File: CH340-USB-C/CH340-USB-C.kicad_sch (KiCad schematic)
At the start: 18 parts, among them J1 USB_C_Receptacle_USB2.0, J2 Conn_01x04_MountingPin, SW1 SW_Push_SPDT, U1 XC6206PxxxMR, U2 CH340N

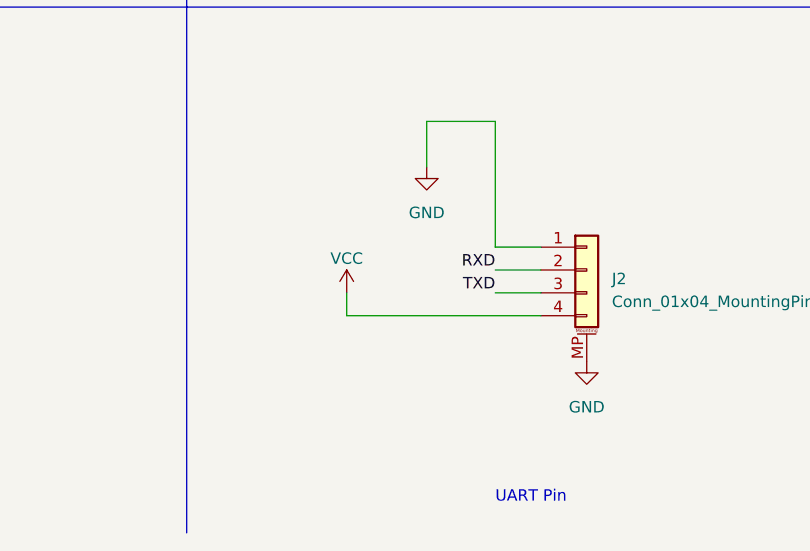
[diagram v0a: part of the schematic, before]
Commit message: 新增
1.可以選擇是否輸出電源(預設"不輸出")
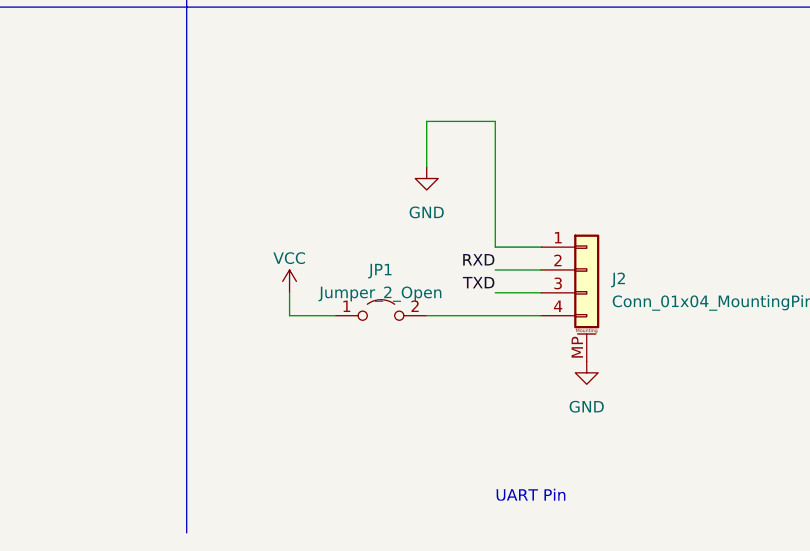
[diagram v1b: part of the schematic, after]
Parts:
- added JP1: Jumper_2_Open, Jumper:SolderJumper-2_P1.3mm_Open_RoundedPad1.0x1.5mm, symbol Jumper:Jumper_2_Open
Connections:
- net VCC: now also JP1.1 (A); no longer J2.4 (Pin_4)
- new net: J2.4 (Pin_4), JP1.2 (B)
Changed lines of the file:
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@@
     (stroke (width 0) (type solid))
   )
-  (wire (pts (xy 115.57 171.45) (xy 115.57 173.99))
+  (wire (pts (xy 109.22 171.45) (xy 109.22 173.99))
     (stroke (width 0) (type default))
   )
@@
     (stroke (width 0) (type default))
   )
+  (wire (pts (xy 114.3 173.99) (xy 109.22 173.99))
+    (stroke (width 0) (type default))
+  )
   (wire (pts (xy 48.26 35.56) (xy 60.96 35.56))
     (stroke (width 0) (type solid))
@@
     (stroke (width 0) (type solid))
   )
-  (wire (pts (xy 137.16 173.99) (xy 115.57 173.99))
+  (wire (pts (xy 137.16 173.99) (xy 124.46 173.99))
     (stroke (width 0) (type default))
   )
@@
     )
   )
+  (symbol (lib_id "Jumper:Jumper_2_Open") (at 119.38 173.99 0) (unit 1)
+    (in_bom yes) (on_board yes) (dnp no) (fields_autoplaced)
+    (property "Reference" "JP1" (at 119.38 168.91 0)
+      (effects (font (size 1.27 1.27)))
+    )
+    (property "Value" "Jumper_2_Open" (at 119.38 171.45 0)
+      (effects (font (size 1.27 1.27)))
+    )
+    (property "Footprint" "Jumper:SolderJumper-2_P1.3mm_Open_RoundedPad1.0x1.5mm" (at 119.38 173.99 0)
+      (effects (font (size 1.27 1.27)) hide)
+    )
+    (property "Datasheet" "~" (at 119.38 173.99 0)
+      (effects (font (size 1.27 1.27)) hide)
+    )
+    (pin "1")
+    (pin "2")
+    (instances
+      (project "CH340-USB-C"
+        (path "/e63e39d7-6ac0-4ffd-8aa3-1841a4541b55"
+          (reference "JP1") (unit 1)
+        )
+      )
+    )
+  )
   (symbol (lib_id "power:GND") (at 142.24 179.07 0) (unit 1)
     (in_bom yes) (on_board yes) (dnp no) (fields_autoplaced)
@@
     )
   )
-  (symbol (lib_id "power:VCC") (at 115.57 171.45 0) (unit 1)
+  (symbol (lib_id "power:VCC") (at 109.22 171.45 0) (unit 1)
     (in_bom yes) (on_board yes) (dnp no) (fields_autoplaced)
-    (property "Reference" "#PWR017" (at 115.57 175.26 0)
-      (effects (font (size 1.27 1.27)) hide)
-    )
-    (property "Value" "VCC" (at 115.57 167.64 0)
-      (effects (font (size 1.27 1.27)))
-    )
-    (property "Footprint" "" (at 115.57 171.45 0)
-      (effects (font (size 1.27 1.27)) hide)
-    )
-    (property "Datasheet" "" (at 115.57 171.45 0)
-      (effects (font (size 1.27 1.27)) hide)
-    )
+    (property "Reference" "#PWR017" (at 109.22 175.26 0)
+      (effects (font (size 1.27 1.27)) hide)
+    )
+    (property "Value" "VCC" (at 109.22 167.64 0)
+      (effects (font (size 1.27 1.27)))
+    )
+    (property "Footprint" "" (at 109.22 171.45 0)
+      (effects (font (size 1.27 1.27)) hide)
+    )
+    (property "Datasheet" "" (at 109.22 171.45 0)
+      (effects (font (size 1.27 1.27)) hide)
+    )

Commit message: 增加絲印
增加公司名稱及腳位名稱
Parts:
- C3, C4: LCSC (none) -> C49678
- JP1, SW1: now left out of the parts list
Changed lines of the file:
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@@
   )
   (symbol (lib_id "Jumper:Jumper_2_Open") (at 119.38 173.99 0) (unit 1)
-    (in_bom yes) (on_board yes) (dnp no) (fields_autoplaced)
+    (in_bom no) (on_board yes) (dnp no) (fields_autoplaced)
     (property "Reference" "JP1" (at 119.38 168.91 0)
       (effects (font (size 1.27 1.27)))
@@
     )
     (property "Datasheet" "~" (at 118.11 52.07 0)
+      (effects (font (size 1.27 1.27)) hide)
+    )
+    (property "LCSC" "C49678" (at 118.11 52.07 0)
       (effects (font (size 1.27 1.27)) hide)
     )
@@
   )
   (symbol (lib_id "Switch:SW_Push_SPDT") (at 142.24 116.84 0) (unit 1)
-    (in_bom yes) (on_board yes) (dnp no)
+    (in_bom no) (on_board yes) (dnp no)
     (property "Reference" "SW1" (at 142.24 109.22 0)
       (effects (font (size 1.27 1.27)))
@@
       (effects (font (size 1.27 1.27)) hide)
     )
+    (property "LCSC" "C49678" (at 124.46 52.07 0)
+      (effects (font (size 1.27 1.27)) hide)
+    )

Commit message: 打樣
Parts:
- C3, C4: LCSC C49678 -> (none)
- J1: LCSC C2765186 -> (none)
- J2: LCSC C722701 -> (none)
- JP1, SW1: now in the parts list
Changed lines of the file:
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@@
       (effects (font (size 1.27 1.27)) hide)
     )
-    (property "LCSC" "C2977777" (at 149.86 49.53 0)
-      (effects (font (size 1.27 1.27)))
+    (property "LCSC" "C2977777" (at 143.51 40.64 0)
+      (effects (font (size 1.27 1.27)) hide)
     )
     (pin "1")
@@
       (effects (font (size 1.27 1.27)) hide)
     )
-    (property "LCSC" "C722701" (at 142.24 168.91 0)
-      (effects (font (size 1.27 1.27)) hide)
-    )
     (pin "1")
     (pin "2")
@@
   )
   (symbol (lib_id "Jumper:Jumper_2_Open") (at 119.38 173.99 0) (unit 1)
-    (in_bom no) (on_board yes) (dnp no) (fields_autoplaced)
+    (in_bom yes) (on_board yes) (dnp no) (fields_autoplaced)
     (property "Reference" "JP1" (at 119.38 168.91 0)
       (effects (font (size 1.27 1.27)))
@@
       (effects (font (size 1.27 1.27)) hide)
     )
-    (property "LCSC" "C49678" (at 118.11 52.07 0)
-      (effects (font (size 1.27 1.27)) hide)
-    )
     (pin "1")
     (pin "2")
@@
     (property "Datasheet" "https://www.usb.org/sites/default/files/documents/usb_type-c.zip" (at 36.83 43.18 0)
       (effects (font (size 1.27 1.27)) hide)
-    )
-    (property "LCSC" "C2765186" (at 39.37 62.23 0)
-      (effects (font (size 1.27 1.27)))
     )
     (pin "A1")
@@
   )
   (symbol (lib_id "Switch:SW_Push_SPDT") (at 142.24 116.84 0) (unit 1)
-    (in_bom no) (on_board yes) (dnp no)
+    (in_bom yes) (on_board yes) (dnp no)
     (property "Reference" "SW1" (at 142.24 109.22 0)
       (effects (font (size 1.27 1.27)))
@@
       (effects (font (size 1.27 1.27)) hide)
     )
-    (property "LCSC" "C49678" (at 124.46 52.07 0)
-      (effects (font (size 1.27 1.27)) hide)
-    )
